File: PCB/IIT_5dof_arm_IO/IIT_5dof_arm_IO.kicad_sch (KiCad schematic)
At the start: 74 parts, among them J1 Conn_01x05, J10 Conn_01x06, J11 Conn_01x06, J12 Conn_01x06, J13 Conn_01x06, J2 Conn_01x03, J3 Conn_02x03_Counter_Clockwise, J4 Conn_01x03, J5 Conn_01x04, J6 Conn_01x04, J7 Conn_02x13_Top_Bottom, J8 Conn_01x06, J9 Conn_01x06, Q1 2N7002, SW1 SW_Push, SW10 SW_Push, SW11 SW_Push, SW12 SW_Push, SW13 SW_Push, SW14 SW_Push, SW2 SW_Push, SW3 SW_Push, SW4 SW_Push, SW5 SW_Push, SW6 SW_Push, SW7 RotaryEncoder_Switch, SW8 SW_Push, SW9 SW_Push, U1 ATmega328P-A, Y1 16MHz

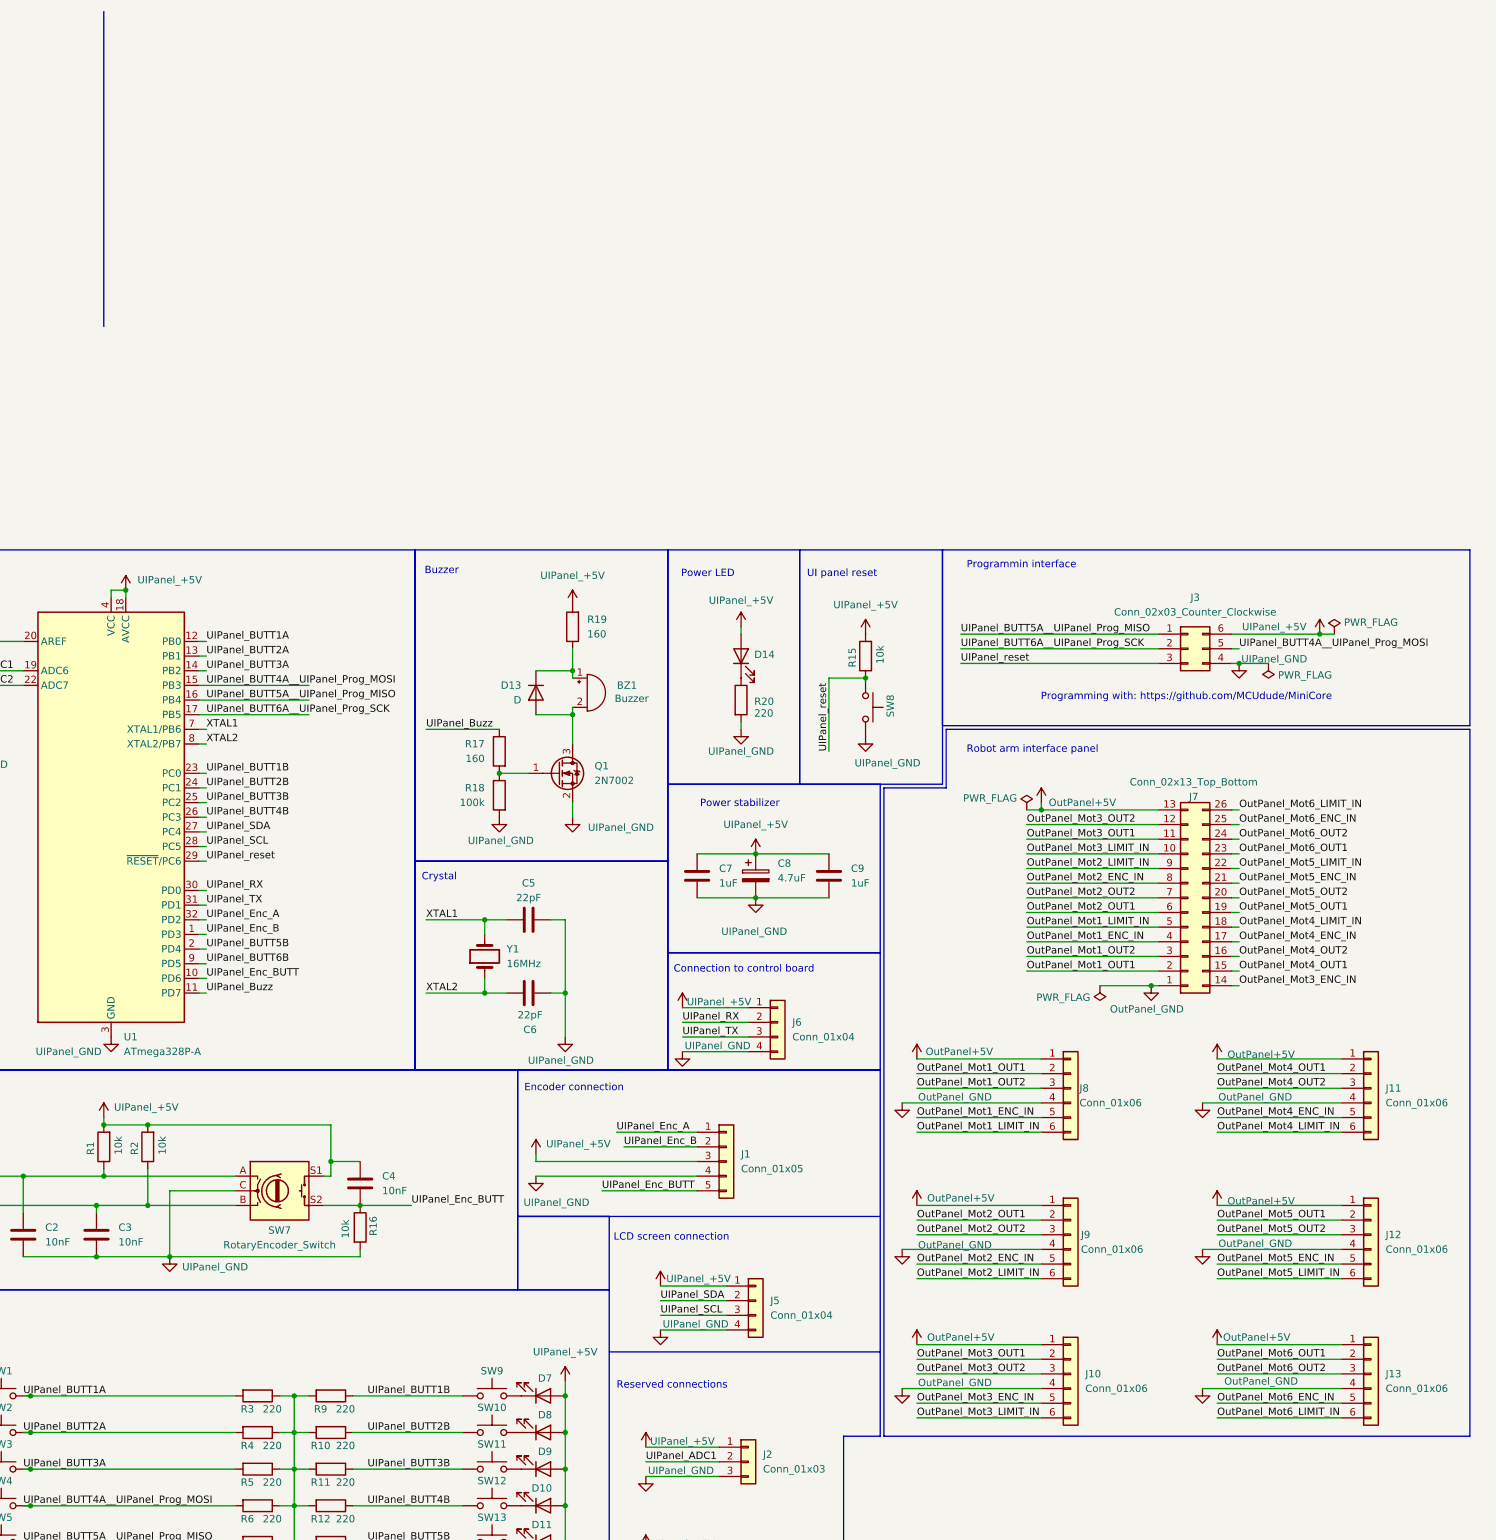
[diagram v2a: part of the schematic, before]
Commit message: Add RS-232 interface
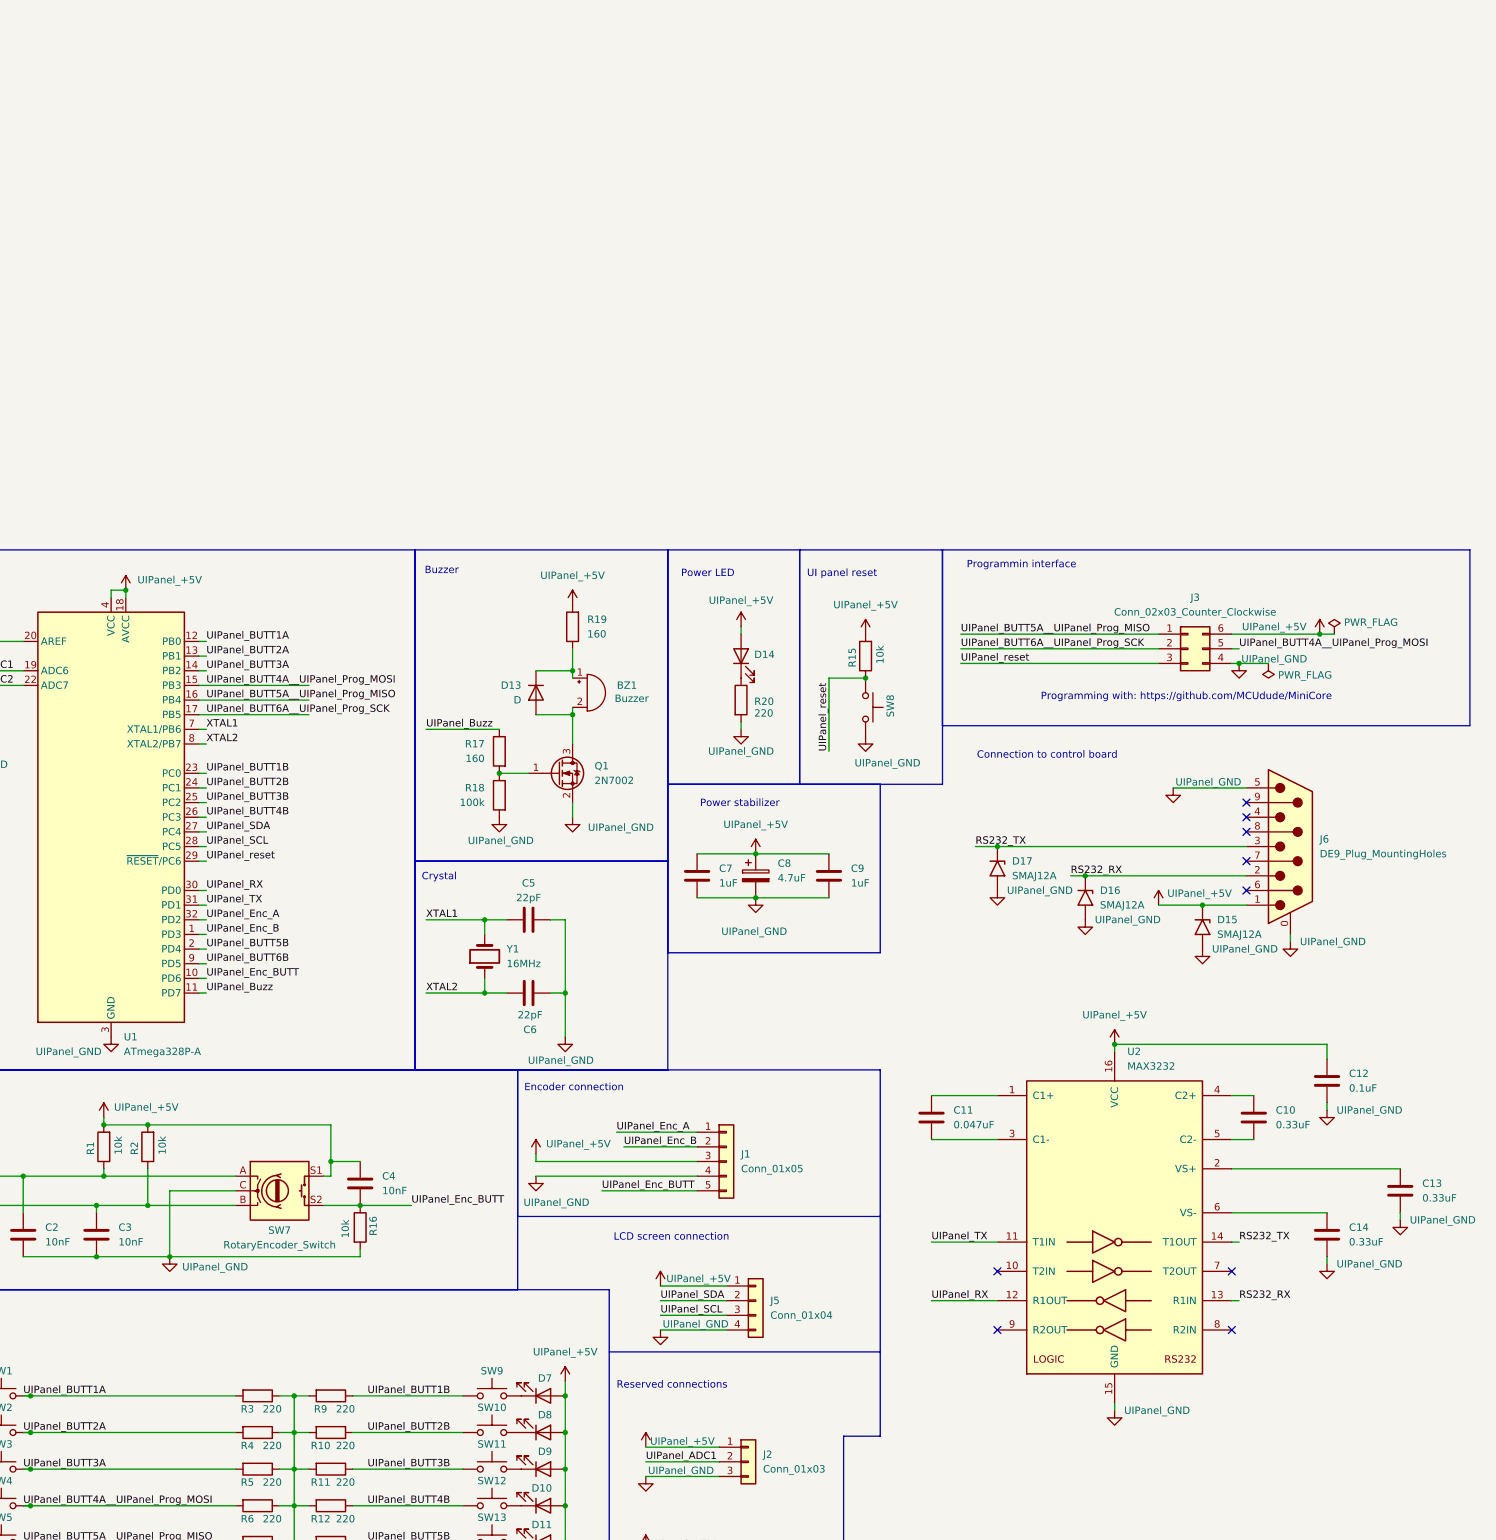
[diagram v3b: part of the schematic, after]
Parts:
- removed J10, J11, J12, J13, J8, J9: Conn_01x06, Connector_Molex:Molex_KK-254_AE-6410-06A_1x06_P2.54mm_Vertical, symbol Connector_Generic:Conn_01x06
- removed J6: Conn_01x04, Connector_Molex:Molex_KK-254_AE-6410-04A_1x04_P2.54mm_Vertical, symbol Connector_Generic:Conn_01x04
- removed J7: Conn_02x13_Top_Bottom, Connector_IDC:IDC-Header_2x13_P2.54mm_Vertical, symbol Connector_Generic:Conn_02x13_Top_Bottom
- added C10, C13, C14: 0.33uF, symbol Device:C
- added C11: 0.047uF, symbol Device:C
- added C12: 0.1uF, symbol Device:C
- added D15, D16, D17: SMAJ12A, Diode_SMD:D_SMA, symbol Diode:SMAJ12A
- added J6: DE9_Plug_MountingHoles, symbol Connector:DE9_Plug_MountingHoles
- added U2: MAX3232, symbol Interface_UART:MAX3232
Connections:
- net UIPanel_+5V: now also C12.1, D15.1 (A1), J6.1, U2.16 (VCC)
- net UIPanel_GND: now also C12.2, C13.2, C14.2, D15.2 (A2), D16.2 (A2), D17.2 (A2), J6.0 (PAD), J6.5, U2.15 (GND)
- net UIPanel_RX: now also U2.12 (R1OUT)
- net UIPanel_TX: now also U2.11 (T1IN)
- new net: C10.1, U2.4 (C2+)
- new net: C10.2, U2.5 (C2-)
- new net: C14.1, U2.6 (VS-)
- new net: C11.1, U2.1 (C1+)
- new net: C13.1, U2.2 (VS+)
- new net: C11.2, U2.3 (C1-)
- new net RS232_RX: D16.1 (A1), J6.2, U2.13 (R1IN)
- new net RS232_TX: D17.1 (A1), J6.3, U2.14 (T1OUT)
- no-connect marks 0 -> 9
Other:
- note removed: "Robot arm interface panel"

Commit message: Improve LED button pullups + add detach MOSFETs
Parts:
- added F1: 1812L050PR, symbol Device:Polyfuse
- added Q2, Q3, Q4: 2N7002, Package_TO_SOT_SMD:SOT-23, symbol Transistor_FET:2N7002
- added R23, R24, R25, R26, R27, R28, R29, R30, R31, R32, R33, R34, R35, R36, R37: 10k, Resistor_SMD:R_0805_2012Metric_Pad1.20x1.40mm_HandSolder, symbol Device:R
- added SW15: SW_SPDT, symbol Switch:SW_SPDT
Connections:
- net UIPanel_+5V: now also F1.2, R23.1, R24.1, R25.1, R26.1, R27.1, R28.1, R29.1, R30.1, R31.1, R32.1, R33.1, R34.1, R35.1, R36.1, R37.1; no longer J6.1
- net UIPanel_BUTT1A: now also R24.2
- net UIPanel_BUTT1B: now also R9.2, SW9.1, R31.2; no longer R9.1, SW9.2
- net UIPanel_BUTT2A: now also R25.2
- net UIPanel_BUTT2B: now also R10.2, SW10.1, R32.2; no longer R10.1, SW10.2
- net UIPanel_BUTT3A: now also R26.2
- net UIPanel_BUTT3B: now also R11.2, SW11.1, R33.2; no longer R11.1, SW11.2
- net UIPanel_BUTT4B: now also R12.2, SW12.1, R37.2; no longer R12.1, SW12.2
- net UIPanel_BUTT5A__UIPanel_Prog_MISO: now also Q3.2 (S); no longer R7.2
- net UIPanel_BUTT5B: now also R13.2, SW13.1, R34.2; no longer R13.1, SW13.2
- net UIPanel_BUTT6A__UIPanel_Prog_SCK: now also Q2.2 (S); no longer R8.2
- net UIPanel_GND: now also SW1.1, SW10.2, SW11.2, SW12.2, SW13.2, SW14.2, SW2.1, SW3.1, SW4.1, SW5.1, SW6.1, SW9.2, SW15.3 (C); no longer R10.2, R11.2, R12.2, R13.2, R14.2, R3.1, R4.1, R5.1, R6.1, R7.1, R8.1, R9.2
- net at D2.1 (K): now also R4.1; no longer SW2.1
- net at D6.1 (K): now also R8.1; no longer SW6.1
- net at D3.1 (K): now also R5.1; no longer SW3.1
- net at D12.1 (K): now also R14.1; no longer SW14.1
- net at D7.1 (K): now also R9.1; no longer SW9.1
- net at D5.1 (K): now also R7.1; no longer SW5.1
- net at D10.1 (K): now also R12.1; no longer SW12.1
- net at D8.1 (K): now also R10.1; no longer SW10.1
- net at D4.1 (K): now also R6.1; no longer SW4.1
- net at D11.1 (K): now also R13.1; no longer SW13.1
- net at D1.1 (K): now also R3.1; no longer SW1.1
- net at D9.1 (K): now also R11.1; no longer SW11.1
- net UIPanel_BUTT4A__UIPanel_Prog_MOSI renamed UIPanel_BUTT4A
- net UIPanel_BUTT4A: now also U1.9 (PD5), R27.2; no longer J3.5 (Pin_5), U1.15 (PB3)
- removed net UIPanel_BUTT6B: R14.1, SW14.2, U1.9 (PD5)
- new net: Q3.3 (D), R28.2, R7.2
- new net: Q2.3 (D), R29.2, R8.2
- new net: F1.1, J6.1
- new net: Q4.3 (D), R14.2, R35.2
- new net PROG_SW: Q2.1 (G), Q3.1 (G), Q4.1 (G), R23.2, R30.2, R36.2, SW15.2 (B)
- new net UIPanel_BUTT6B__UIPanel_Prog_MOSI: J3.5 (Pin_5), Q4.2 (S), SW14.1, U1.15 (PB3)
- no-connect marks 9 -> 10
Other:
- note added: "Pullup part can be deconnected throuh MOS FETs while programming"
- moved on the sheet: C10, C11, C12, C13, C14, C2, C3, C4, C7, C8, C9, D1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

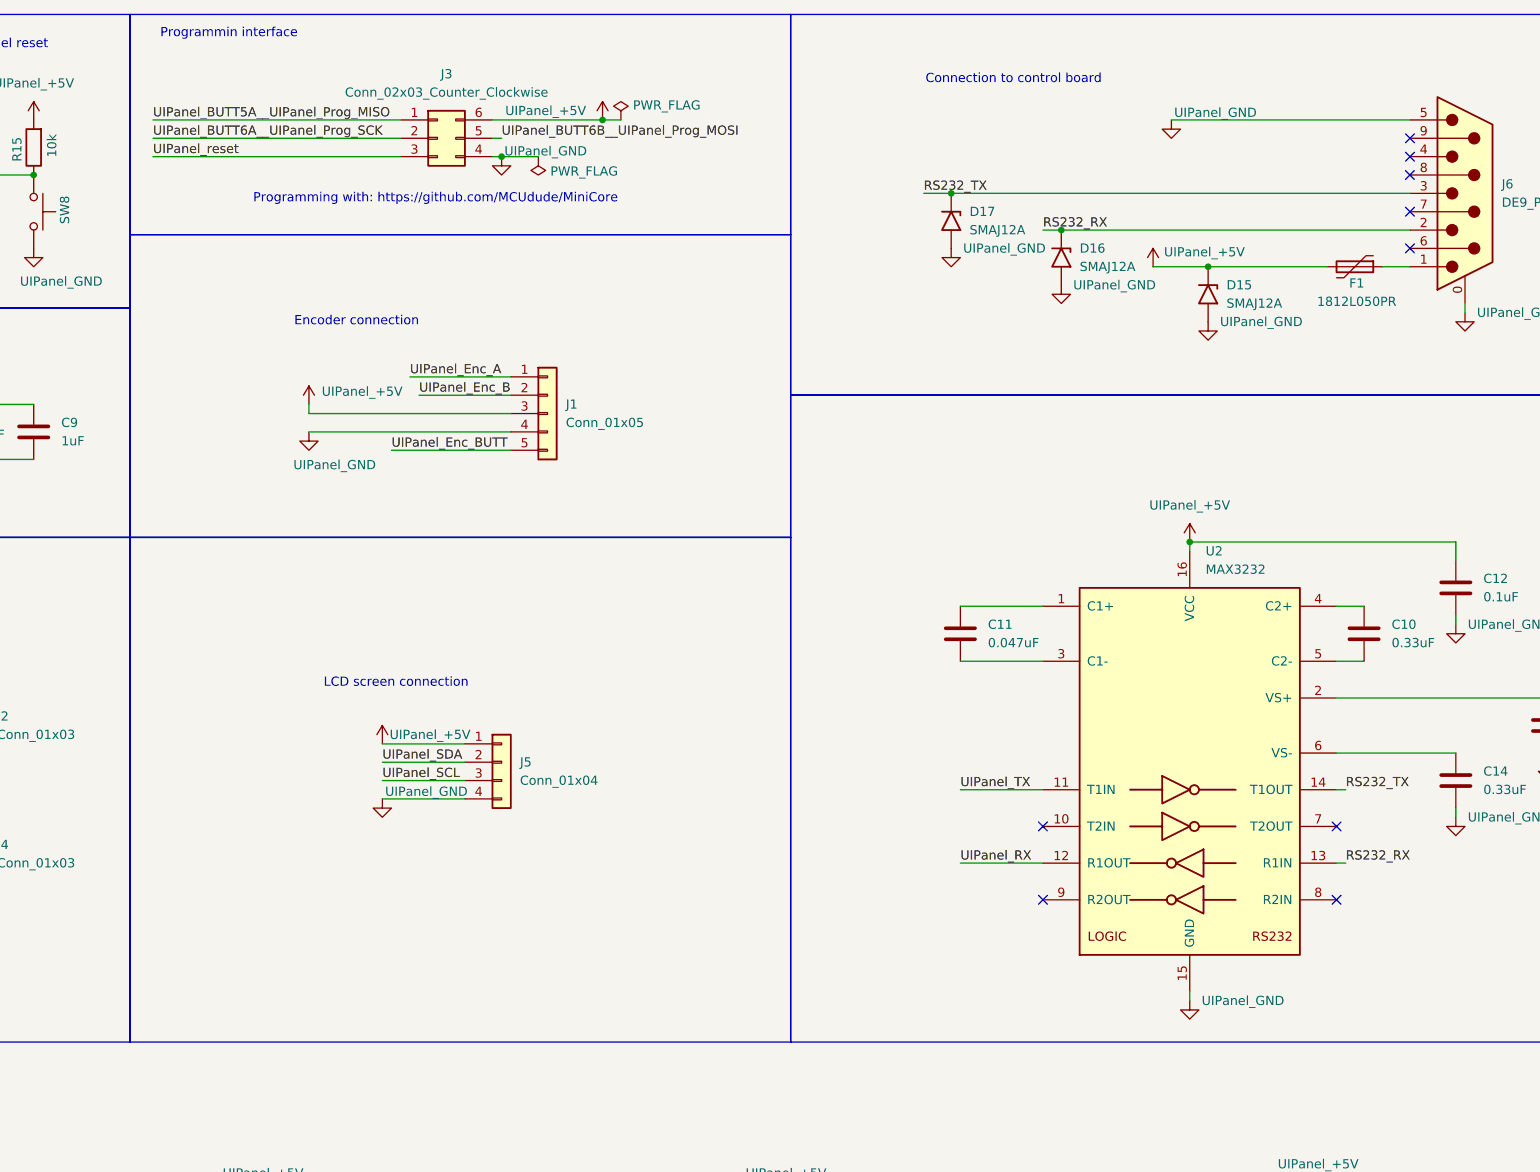
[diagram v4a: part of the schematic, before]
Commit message: Add fuse, footprint assignment, minor tidy up
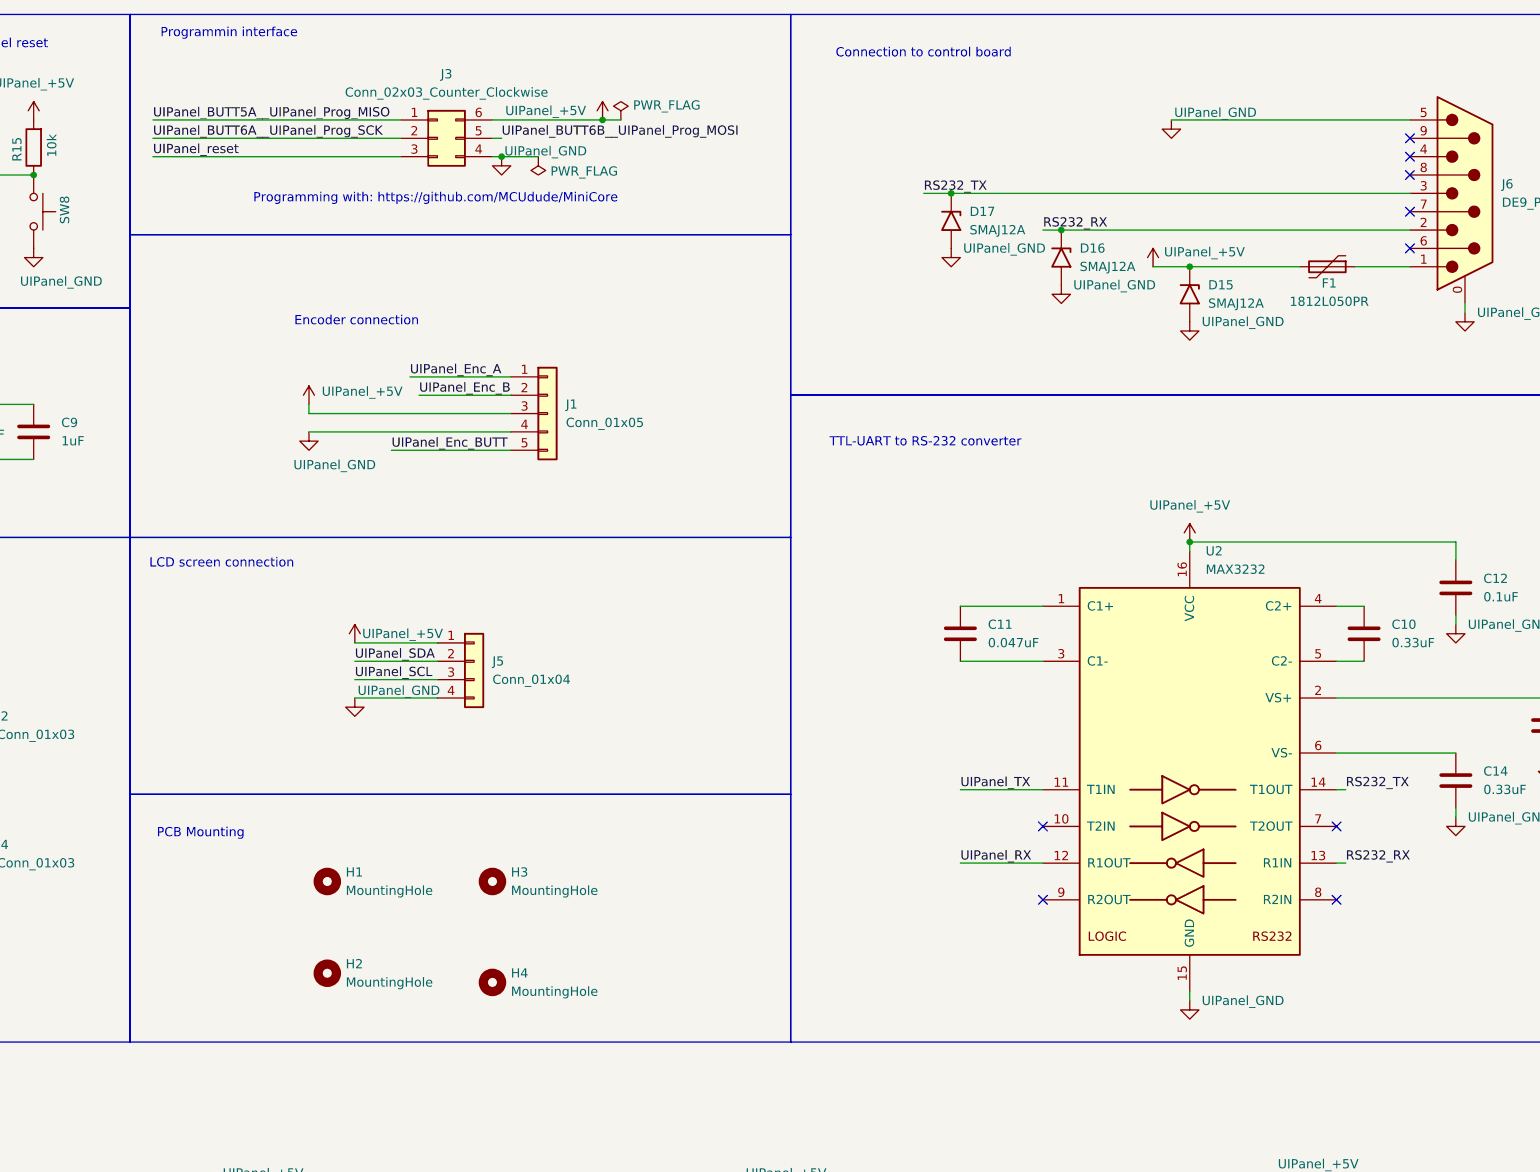
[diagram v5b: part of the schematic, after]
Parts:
- added H1, H2, H3, H4: MountingHole, MountingHole:MountingHole_3.2mm_M3, symbol Mechanical:MountingHole
- C10, C11, C12, C13, C14: footprint (none) -> Capacitor_SMD:C_0805_2012Metric_Pad1.18x1.45mm_HandSolder
- F1: footprint (none) -> IIT_5dof_arm_IO:1812L050PR__1.78mm_3.15mm_3.45mm
- J6: footprint (none) -> Connector_Dsub:DSUB-9_Male_Horizontal_P2.77x2.84mm_EdgePinOffset7.70mm_Housed_MountingHolesOffset9.12mm
- SW15: footprint (none) -> Connector_PinHeader_2.54mm:PinHeader_1x03_P2.54mm_Vertical
- U2: footprint (none) -> Package_SO:SOIC-16W_5.3x10.2mm_P1.27mm
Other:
- note added: "PCB Mounting"
- note added: "TTL-UART to RS-232 converter"
- moved on the sheet: D15, F1, J5
